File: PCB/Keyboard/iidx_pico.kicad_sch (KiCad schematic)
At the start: 70 parts, among them J1 CONN_01x05, J2 CONN_01x05, SW1 SWITCH_SPST, SW10 SWITCH_SPST, SW11 SWITCH_SPST, SW12 Tact_4pin, SW13 Tact_4pin, SW2 SWITCH_SPST, SW3 SWITCH_SPST, SW4 SWITCH_SPST, SW5 SWITCH_SPST, SW6 SWITCH_SPST, SW7 SWITCH_SPST, SW8 SWITCH_SPST, SW9 SWITCH_SPST, U1 Pico

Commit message: 3.3 to 5 level shifter added to PCB
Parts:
- removed R1: 220, Resistor_SMD:R_0603_1608Metric, symbol Device:R_Small
- removed R2: 10, Resistor_SMD:R_0603_1608Metric, symbol Device:R_Small
- added U2, U3: SN74LV1T34DBV, iidx_pico:SOT-23-5_Jumper, symbol Logic_LevelTranslator:SN74LV1T34DBV
- renumbered R3 to R1
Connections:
- net +5V: now also U2.5 (VCC), U3.5 (VCC)
- net GND: now also U2.3 (GND), U3.3 (GND)
- net LED2: now also U2.4 (Y)
- net TT_LED: now also U3.4 (Y)
- net at U1.17 (GPIO13): now also U2.2 (A)
- net at U1.34 (GPIO28_ADC2): now also U3.2 (A)

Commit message: Adds 3.5mm 4P jack connection option
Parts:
- added J3: PJ393-8P, iidx_pico:PJ393-8P, symbol Connector:AudioPlug4
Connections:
- net +5V: now also J3.T
- net GND: now also J3.S
- net SDA: now also J3.R2
- net TT_LED: now also J3.R1
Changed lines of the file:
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@@
   (junction (at 64.77 254) (diameter 0) (color 0 0 0 0)
   )
+  (junction (at 275.59 91.44) (diameter 0) (color 0 0 0 0)
+  )
   (junction (at 146.05 203.835) (diameter 0) (color 0 0 0 0)
   )
@@
   (junction (at 117.475 127) (diameter 0) (color 0 0 0 0)
   )
+  (junction (at 270.51 39.37) (diameter 0) (color 0 0 0 0)
+  )
   (junction (at 58.42 189.23) (diameter 0) (color 0 0 0 0)
   )
@@
   )
   (junction (at 118.11 224.79) (diameter 0) (color 0 0 0 0)
+  )
+  (junction (at 279.4 96.52) (diameter 0) (color 0 0 0 0)
   )
   (no_connect (at 104.14 67.31))
@@
   (no_connect (at 209.55 121.92))
   (no_connect (at 209.55 124.46))
-  (wire (pts (xy 257.81 91.44) (xy 285.75 91.44))
+  (wire (pts (xy 257.81 91.44) (xy 275.59 91.44))
     (stroke (width 0) (type default) (color 0 0 0 0))
   )
@@
     (stroke (width 0) (type default) (color 0 0 0 0))
   )
+  (wire (pts (xy 275.59 91.44) (xy 285.75 91.44))
+    (stroke (width 0) (type default) (color 0 0 0 0))
+  )
   (wire (pts (xy 209.55 119.38) (xy 236.22 119.38))
     (stroke (width 0) (type default) (color 0 0 0 0))
@@
     (stroke (width 0) (type default) (color 0 0 0 0))
   )
+  (wire (pts (xy 270.51 39.37) (xy 292.1 39.37))
+    (stroke (width 0) (type default) (color 0 0 0 0))
+  )
   (wire (pts (xy 127.635 123.19) (xy 127.635 127))
     (stroke (width 0) (type default) (color 0 0 0 0))
@@
     (stroke (width 0) (type default) (color 0 0 0 0))
   )
+  (wire (pts (xy 279.4 96.52) (xy 279.4 44.45))
+    (stroke (width 0) (type default) (color 0 0 0 0))
+  )
   (wire (pts (xy 183.515 220.98) (xy 183.515 232.41))
     (stroke (width 0) (type default) (color 0 0 0 0))
@@
     (stroke (width 0) (type default) (color 0 0 0 0))
   )
-  (wire (pts (xy 260.35 96.52) (xy 299.085 96.52))
+  (wire (pts (xy 260.35 96.52) (xy 279.4 96.52))
     (stroke (width 0) (type default) (color 0 0 0 0))
   )
@@
     (stroke (width 0) (type default) (color 0 0 0 0))
   )
+  (wire (pts (xy 275.59 91.44) (xy 275.59 41.91))
+    (stroke (width 0) (type default) (color 0 0 0 0))
+  )
   (wire (pts (xy 229.87 220.98) (xy 229.87 232.41))
     (stroke (width 0) (type default) (color 0 0 0 0))
@@
     (stroke (width 0) (type default) (color 0 0 0 0))
   )
+  (wire (pts (xy 279.4 44.45) (xy 292.1 44.45))
+    (stroke (width 0) (type default) (color 0 0 0 0))
+  )
   (wire (pts (xy 189.23 71.12) (xy 189.23 54.61))
     (stroke (width 0) (type default) (color 0 0 0 0))
@@
     (stroke (width 0) (type default) (color 0 0 0 0))
   )
+  (wire (pts (xy 292.1 49.53) (xy 292.1 46.99))
+    (stroke (width 0) (type default) (color 0 0 0 0))
+  )
   (wire (pts (xy 170.18 93.98) (xy 173.99 93.98))
     (stroke (width 0) (type default) (color 0 0 0 0))
@@
     (stroke (width 0) (type default) (color 0 0 0 0))
   )
+  (wire (pts (xy 279.4 96.52) (xy 299.085 96.52))
+    (stroke (width 0) (type default) (color 0 0 0 0))
+  )
   (wire (pts (xy 298.45 173.99) (xy 311.15 173.99))
+    (stroke (width 0) (type default) (color 0 0 0 0))
+  )
+  (wire (pts (xy 275.59 41.91) (xy 292.1 41.91))
     (stroke (width 0) (type default) (color 0 0 0 0))
   )
@@
     (pin "2")
   )
+  (symbol (lib_id "power:GND") (at 292.1 49.53 0) (unit 1)
+    (in_bom yes) (on_board yes)
+    (property "Reference" "#PWR0119" (id 0) (at 292.1 55.88 0)
+      (effects (font (size 1.27 1.27)) hide)
+    )
+    (property "Value" "GND" (id 1) (at 292.227 53.9242 0))
+    (property "Footprint" "" (id 2) (at 292.1 49.53 0)
+      (effects (font (size 1.27 1.27)) hide)
+    )
+    (property "Datasheet" "" (id 3) (at 292.1 49.53 0)
+      (effects (font (size 1.27 1.27)) hide)
+    )
+    (pin "1")
+  )
   (symbol (lib_name "WS2812B_Unified_6") (lib_id "iidx_pico:WS2812B_Unified") (at 49.53 200.66 0) (unit 1)
     (in_bom yes) (on_board yes)
@@
     (pin "1")
     (pin "2")
+  )
+  (symbol (lib_id "Connector:AudioPlug4") (at 307.34 44.45 180) (unit 1)
+    (in_bom yes) (on_board yes)
+    (property "Reference" "J3" (id 0) (at 301.625 36.195 0)
+      (effects (font (size 1.27 1.27)) (justify left))
+    )
+    (property "Value" "PJ393-8P" (id 1) (at 309.245 49.53 0)
+      (effects (font (size 1.27 1.27)) (justify left))
+    )
+    (property "Footprint" "iidx_pico:PJ393-8P" (id 2) (at 298.45 41.91 0)
+      (effects (font (size 1.27 1.27)) hide)
+    )
+    (property "Datasheet" "~" (id 3) (at 298.45 41.91 0)
+      (effects (font (size 1.27 1.27)) hide)
+    )
+    (pin "R1")
+    (pin "R2")
+    (pin "S")
+    (pin "T")
   )
   (symbol (lib_id "power:+5V") (at 180.975 144.78 0) (unit 1)
@@
       (reference "#PWR0118") (unit 1) (value "GND") (footprint "")
     )
+    (path "/7c982ea8-03c8-4618-afad-a138dfa76f86"
+      (reference "#PWR0119") (unit 1) (value "GND") (footprint "")
+    )
     (path "/19ea96f8-4372-411f-a3dc-9dd5232e0e1f"
       (reference "C1") (unit 1) (value "1uF") (footprint "Capacitor_SMD:C_0805_2012Metric")
@@
       (reference "J2") (unit 1) (value "CONN_01x05") (footprint "iidx_pico:Pogo_5P_Female")
     )
+    (path "/aa2501f5-ea48-484c-b23d-ec5a6fc97fb1"
+      (reference "J3") (unit 1) (value "PJ393-8P") (footprint "iidx_pico:PJ393-8P")
+    )
     (path "/7ae58c25-a25e-4e23-a224-70a97283316d"

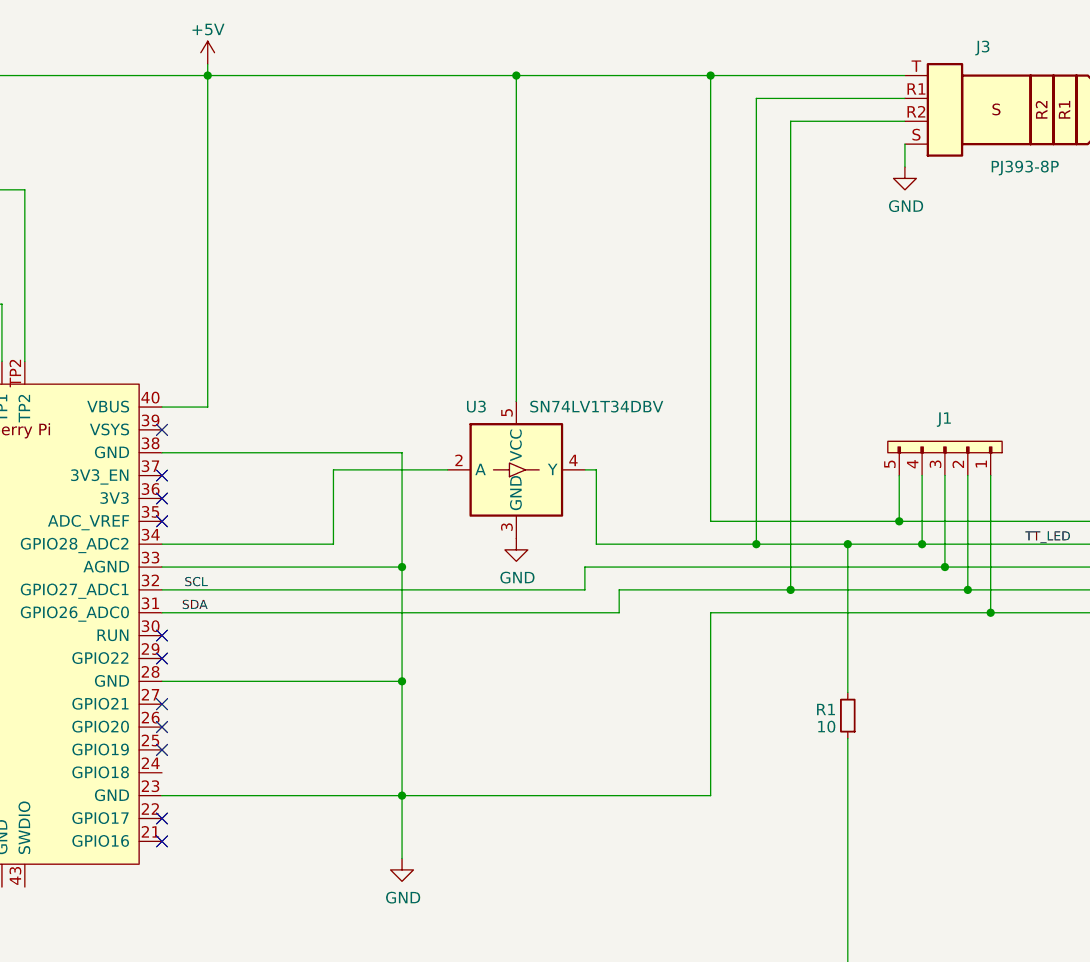
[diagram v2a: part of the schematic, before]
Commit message: Add TVS diode and filter capacitor to PCB
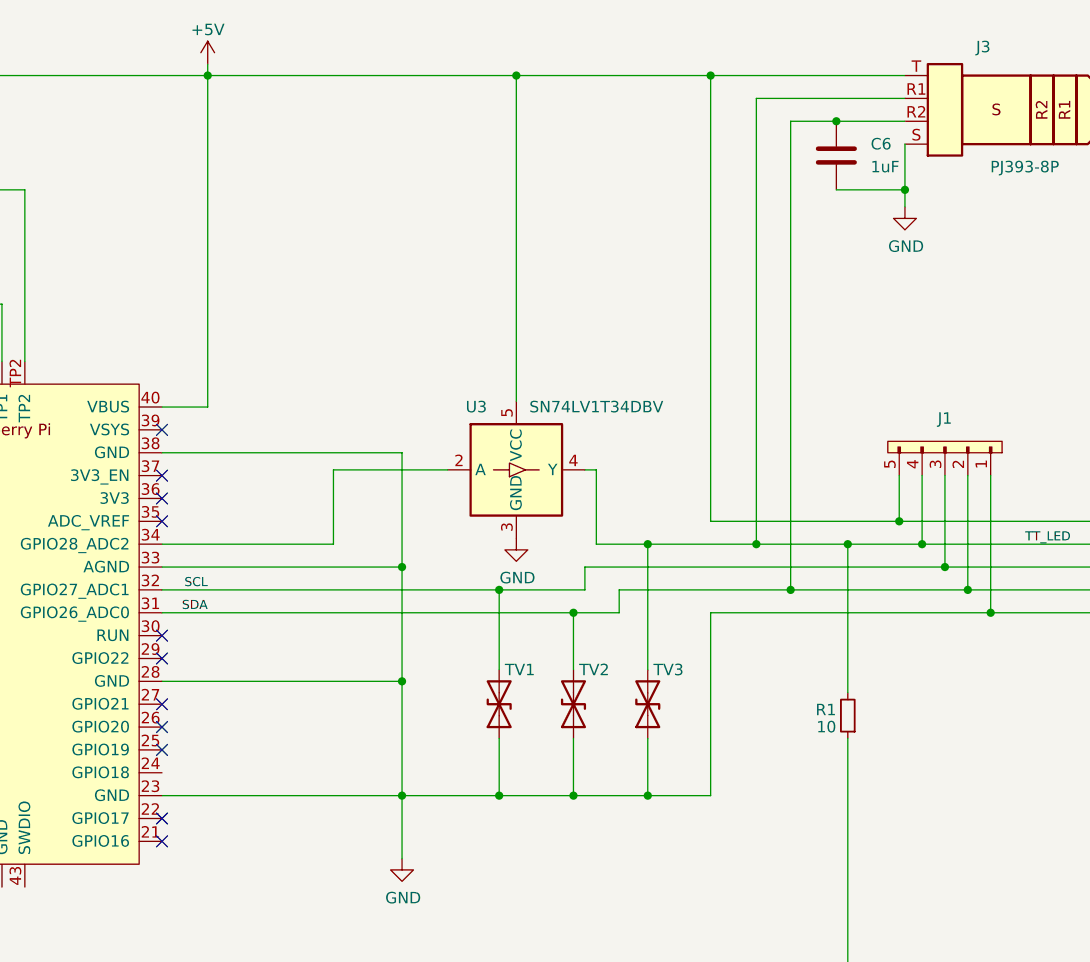
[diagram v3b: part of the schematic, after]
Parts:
- added C6: 1uF, Capacitor_SMD:C_0805_2012Metric, symbol Device:C
- added TV1, TV2, TV3: D_TVS, Diode_SMD:D_SOD-323_HandSoldering, symbol Device:D_TVS
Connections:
- net GND: now also C6.2, TV1.1 (A1), TV2.1 (A1), TV3.1 (A1)
- net SCL: now also TV1.2 (A2)
- net SDA: now also C6.1, TV2.2 (A2)
- net TT_LED: now also TV3.2 (A2)

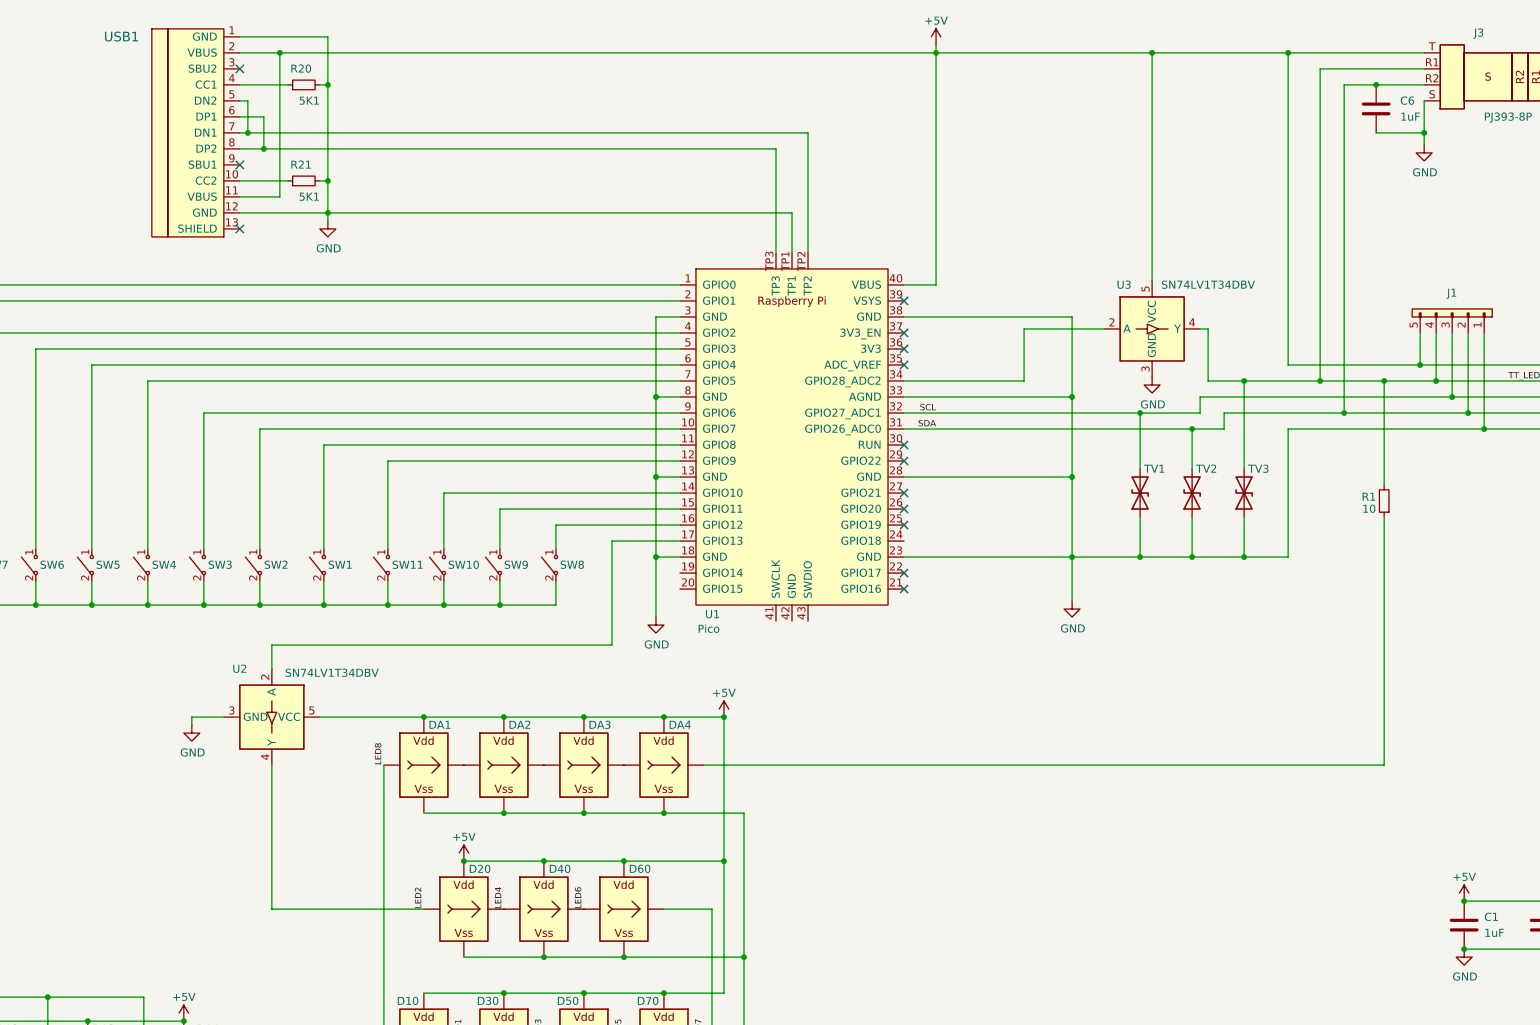
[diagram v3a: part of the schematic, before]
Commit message: Resistors to bypass level shifter
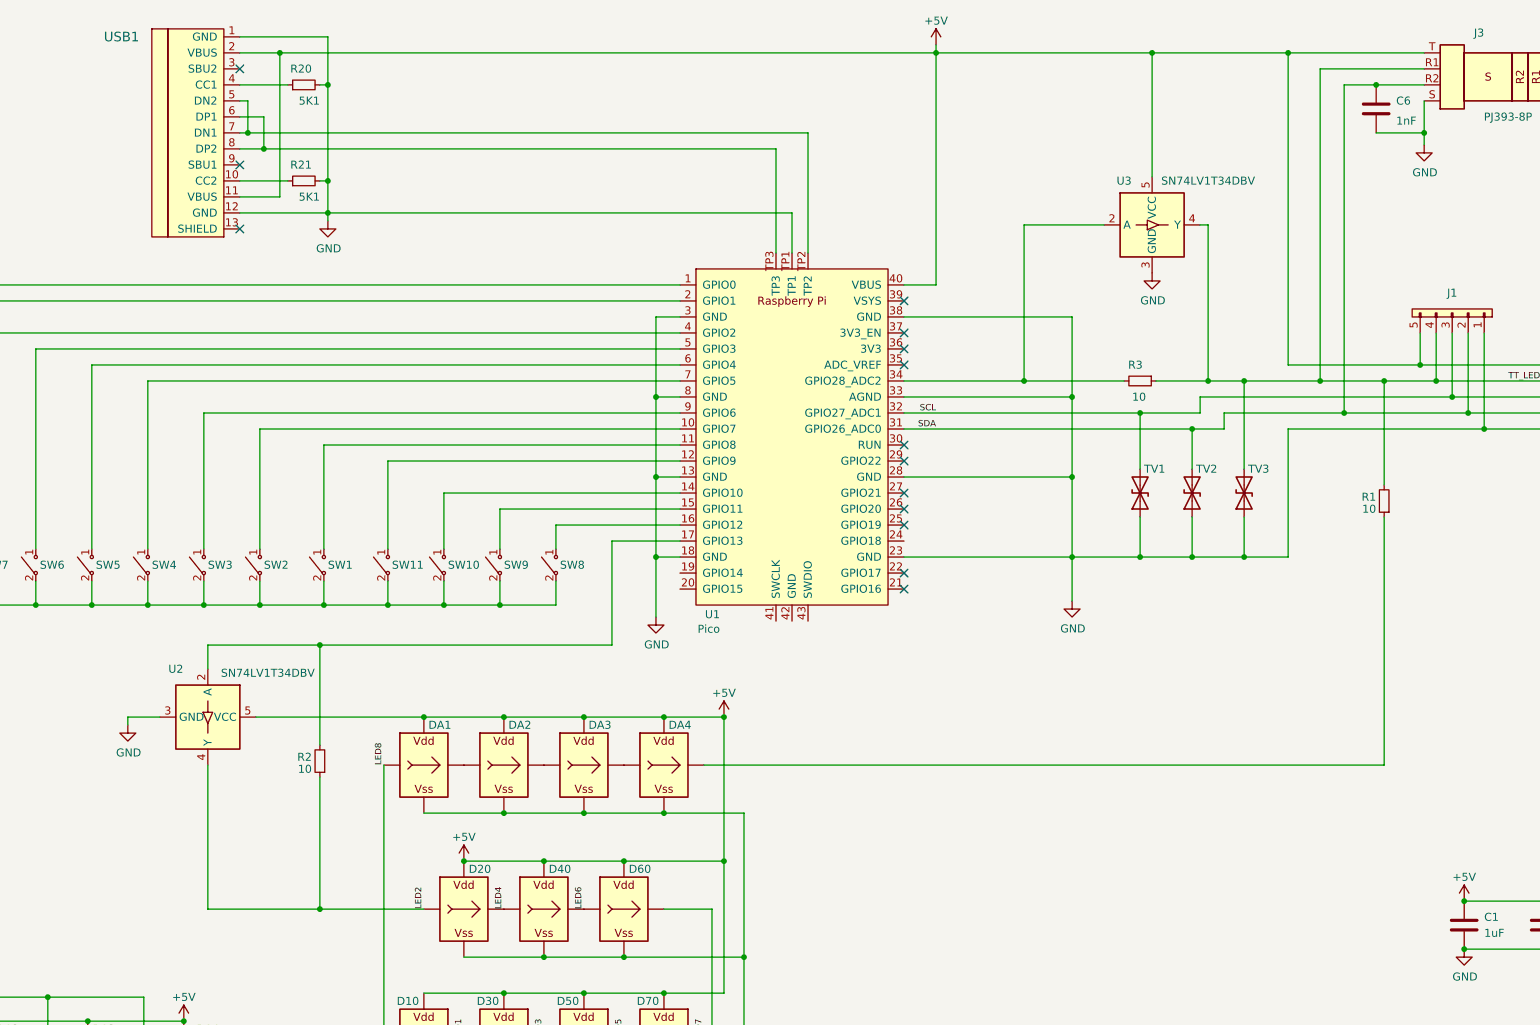
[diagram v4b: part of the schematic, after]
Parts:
- added R2, R3: 10, Resistor_SMD:R_0603_1608Metric, symbol Device:R_Small
- C6: value 1uF -> 1nF
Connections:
- net LED2: now also R2.1
- net TT_LED: now also R3.1
- net at U1.17 (GPIO13), U2.2 (A): now also R2.2
- net at U1.34 (GPIO28_ADC2), U3.2 (A): now also R3.2
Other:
- moved on the sheet: U2, U3
